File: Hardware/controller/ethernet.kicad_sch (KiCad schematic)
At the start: 18 parts, among them U401 KSZ8041TL, X401 50MHz

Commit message: Controller board fan controller
- Added a fan controller (the same EMC2101-R as on the driver) to the
  controller board, to control the rear case fan. This is driven off the
  rear IO I2C bus, which itself is switched behind the "auxiliary" I2C
  bus.
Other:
- title: Ethernet PHY -> Processor Complex – Ethernet PHY
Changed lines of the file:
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@@
   (paper "A4")
   (title_block
-    (title "Ethernet PHY")
+    (title "Processor Complex – Ethernet PHY")
     (date "2022-03-06")
     (rev "1")

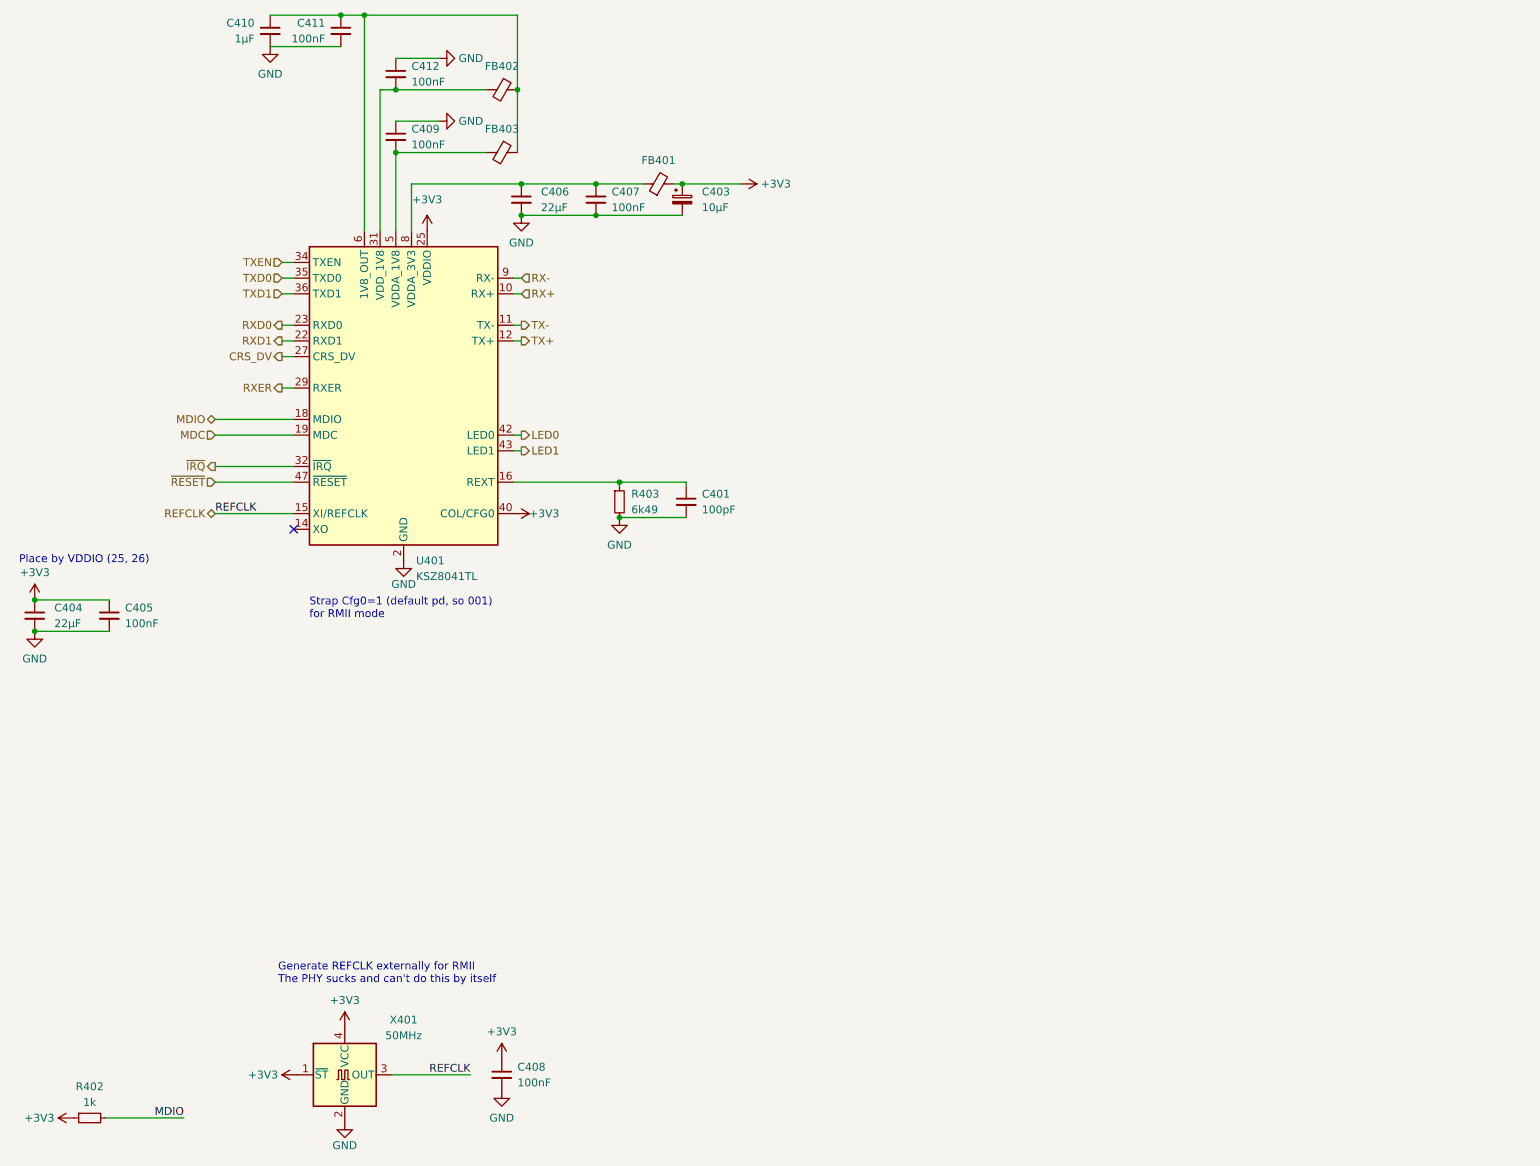
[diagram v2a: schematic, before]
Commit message: Re-design around STM32MP1 (#2)
* Start work on rev3 hardware

- This fits the Technomet R110 enclosure and supports multiple load
  boards, connected via CAN rather than I2C. Each load has a
  microcontroller of its own.

* More new layout stuff

- More work on the new controller board layout

- Rework rear IO board for the new Technomet rear panel (it has an
  expansion connector for CAN also, and features four screw holes
  instead of two)

- Added a few footprints (expansion RJ45 connector; some
  horizontal/vertical headers)

* Work on controller VSense, power

- Routed 3V3 switching supply

- Created footprint and symbols for Kemet EA2 series latching relay

- Added relays to controller to handle routing of voltage sense inputs
  to the sampling ADC

* Rear IO rework

- Mostly finished the rear IO board rework (adding the CAN filtering and
  switchable termination; trigger input pulse shaper; fuses for
  expansion +12V)

- Changed encoder type on front panel for a shorter type

- Created schematic models and footprints for Bournds DR311 chokes;
  Mill-Max 2108 solder turrets

* More work on new controller board

- Switched mains connection for a push-in screw terminal, rather than a
  pluggable block (takes up less space, less parts)

- Added input terminal for rear VSense inputs

- Added -5V supply (same circuit as on analog board; required for
  voltage input sense)

- Replaced beeper with a side-firing version. It takes up a bunch less
  space vertically, and also now added a resistor to (hopefully) make it
  somewhat more quiet

- Added connector for bonus displays

* Add "bonus display" board

- Created the bonus display board, which houses a chip-on-glass 4x10
  text character display. It's meant to be mounted next to the input
  jacks to show a constant location of current/voltage, even if the main
  display is used for menus or other stuff.

- More tweaks to controller board, to do with power g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
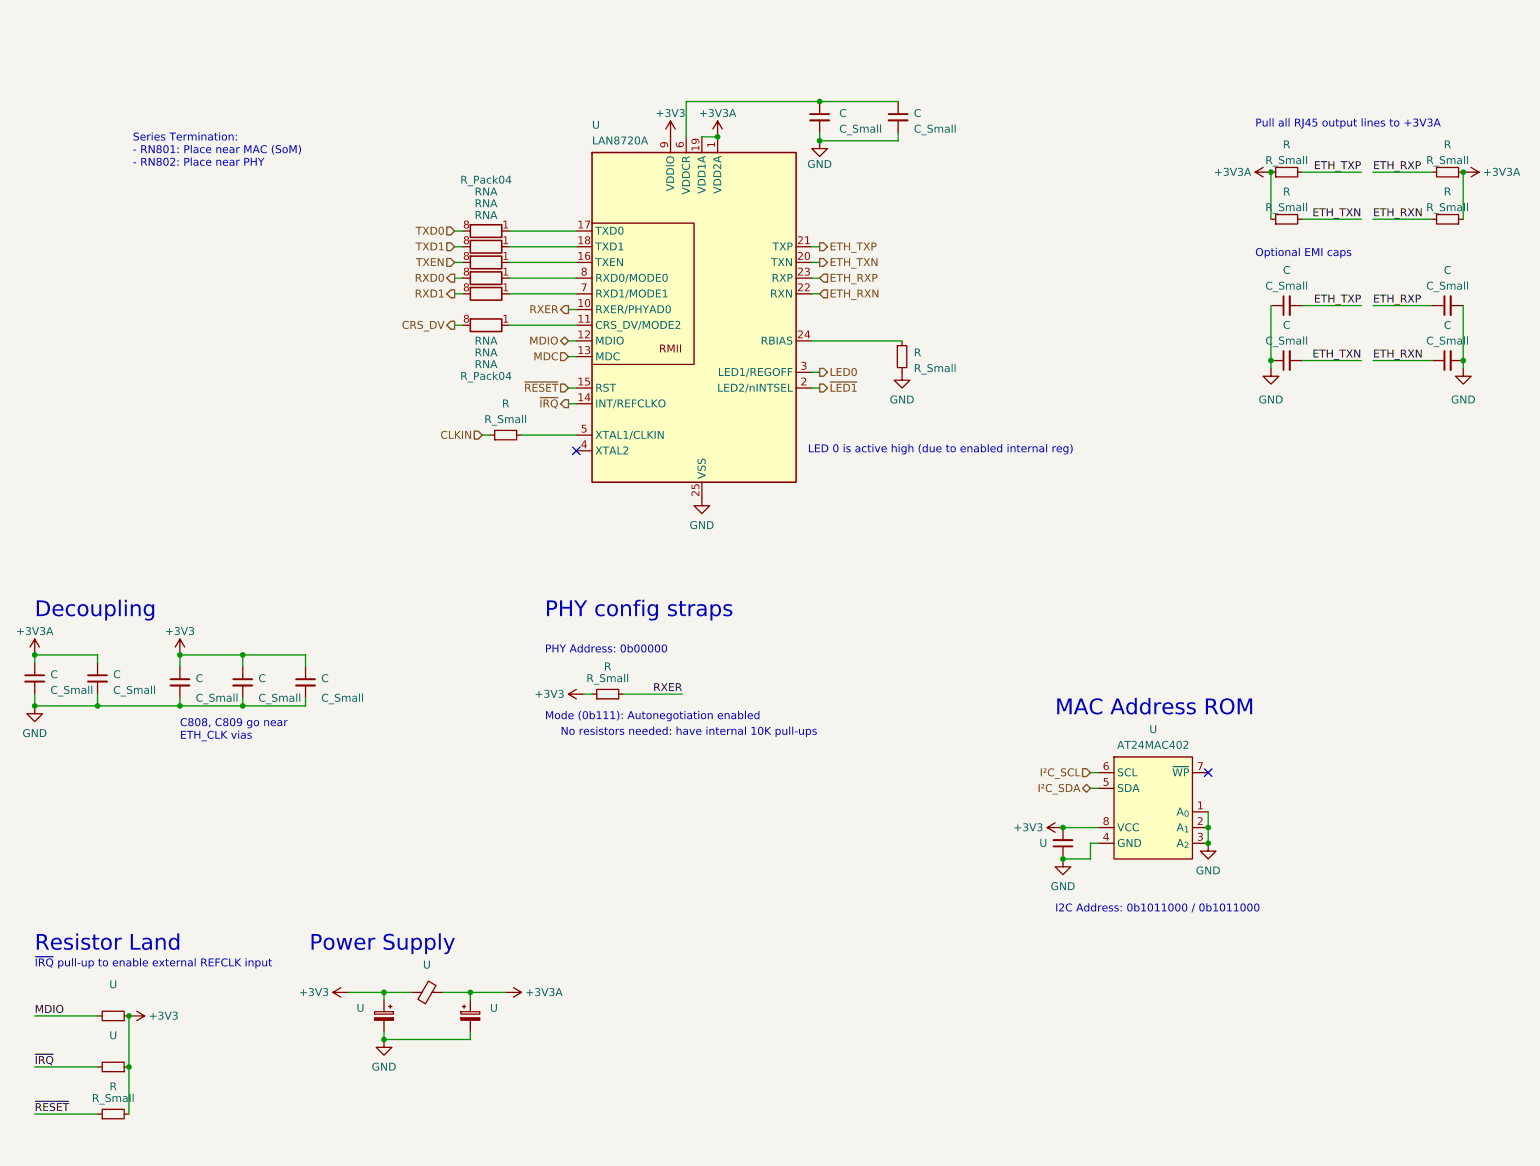
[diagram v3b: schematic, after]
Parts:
- removed C401: 100pF, Capacitor_SMD:C_0805_2012Metric_Pad1.18x1.45mm_HandSolder, symbol Device:C_Small
- removed C403: 10µF, Capacitor_Tantalum_SMD:CP_EIA-3216-18_Kemet-A_Pad1.58x1.35mm_HandSolder, symbol Device:C_Polarized_Small
- removed C404, C406: 22µF, Capacitor_SMD:C_0805_2012Metric_Pad1.18x1.45mm_HandSolder, symbol Device:C_Small
- removed C405, C407, C408, C409, C411, C412: 100nF, Capacitor_SMD:C_0805_2012Metric_Pad1.18x1.45mm_HandSolder, symbol Device:C_Small
- removed C410: 1µF, Capacitor_SMD:C_0805_2012Metric_Pad1.18x1.45mm_HandSolder, symbol Device:C_Small
- removed FB401, FB402, FB403: FerriteBead_Small, Inductor_SMD:L_0805_2012Metric_Pad1.05x1.20mm_HandSolder, symbol Device:FerriteBead_Small
- removed R402: 1k, Resistor_SMD:R_0805_2012Metric_Pad1.20x1.40mm_HandSolder, symbol Device:R_Small
- removed R403: 6k49, Resistor_SMD:R_0805_2012Metric_Pad1.20x1.40mm_HandSolder, symbol Device:R_Small
- removed U401: KSZ8041TL, Package_QFP:TQFP-48_7x7mm_P0.5mm, symbol programmable-load:KSZ8041TL
- removed X401: 50MHz, Oscillator:Oscillator_SMD_SeikoEpson_SG8002LB-4Pin_5.0x3.2mm, symbol Oscillator:SG-5032CAN
- added C (x11): C_Small, symbol Device:C_Small
- added R (x8): R_Small, symbol Device:R_Small
- added RN (x6): R_Pack04, symbol Device:R_Pack04_Split
- added U (x2): (no value), symbol Device:C_Polarized_Small
- added U: LAN8720A, Package_DFN_QFN:QFN-24-1EP_4x4mm_P0.5mm_EP2.6x2.6mm, symbol Interface_Ethernet:LAN8720A
- added U: (no value), symbol Device:FerriteBead_Small
- added U (x2): (no value), symbol Device:R_Small
- added U: (no value), symbol Device:C_Small
- added U: AT24MAC402, Package_SO:TSSOP-8_4.4x3mm_P0.65mm, symbol programmable-load:AT24MAC402
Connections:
- net +3V3: now also C.1, C.1, C.1, R.1, R.2, U.1, U.1, U.1, U.1, U.2, U.8 (VCC), U.9 (VDDIO)
- net CRS_DV: now also RN.8 (R1.2)
- net GND: now also C.1, C.1, C.2, C.2, C.2, C.2, C.2, C.2, C.2, C.2, C.2, R.2, U.1, U.1 (A_{0}), U.2, U.2, U.2 (A_{1}), U.25 (VSS), U.3 (A_{2}), U.4 (GND)
- net LED0: now also U.3 (LED1/REGOFF)
- net MDC: now also U.13 (MDC)
- net MDIO: now also U.12 (MDIO), U.2
- net RXD0: now also RN.8 (R1.2)
- net RXD1: now also RN.8 (R1.2)
- net RXER: now also R.2, U.10 (RXER/PHYAD0)
- net TXD0: now also RN.8 (R1.2)
- net TXD1: now also RN.8 (R1.2)
- net TXEN: now also RN.8 (R1.2)
- net ~{IRQ}: now also U.14 (INT/REFCLKO), U.2
- net ~{RESET}: now also R.1, U.15 (RST)
- new net: R.1, U.24 (RBIAS)
- new net: C.1, C.1, U.6 (VDDCR)
- new net: RN.1 (R1.1), U.11 (CRS_DV/MODE2)
- new net: RN.1 (R1.1), U.16 (TXEN)
- new net: RN.1 (R1.1), U.17 (TXD0)
- new net: RN.1 (R1.1), U.18 (TXD1)
- new net: R.2, U.5 (XTAL1/CLKIN)
- new net: RN.1 (R1.1), U.7 (RXD1/MODE1)
- new net: RN.1 (R1.1), U.8 (RXD0/MODE0)
- new net +3V3A: C.1, C.1, R.1, R.1, R.1, R.1, U.1, U.1 (VDD2A), U.19 (VDD1A), U.2
- new net CLKIN: R.1
- new net ETH_RXN: C.1, R.2, U.22 (RXN)
- new net ETH_RXP: C.1, R.2, U.23 (RXP)
- new net ETH_TXN: C.2, R.2, U.20 (TXN)
- new net ETH_TXP: C.2, R.2, U.21 (TXP)
- new net I²C_SCL : U.6 (SCL)
- new net I²C_SDA: U.5 (SDA)
- new net ~{LED1}: U.2 (LED2/nINTSEL)
- no-connect marks 1 -> 2
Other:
- note added: "C808, C809 go near ETH_CLK vias"
- note added: "Decoupling"
- note added: "I2C Address: 0b1011000 / 0b1011000"
- note added: "LED 0 is active high (due to enabled internal reg)"
- note added: "MAC Address ROM"
- note added: "Mode (0b111): Autonegotiation enabled"
- note added: "No resistors needed: have internal 10K pull-ups"
- note added: "Optional EMI caps"
- note added: "PHY Address: 0b00000"
- note added: "PHY config straps"
- note added: "Power Supply"
- note added: "Pull all RJ45 output lines to +3V3A"
- note added: "Resistor Land"
- note added: "Series Termination: - RN801: Place near MAC (SoM) - RN802: Place near PHY"
- note added: "~{IRQ} pull-up to enable external REFCLK input"
- note removed: "Generate REFCLK externally for RMII The PHY sucks and can't do this by itself"
- note removed: "Place by VDDIO (25, 26)"
- note removed: "Strap Cfg0=1 (default pd, so 001) for RMII mode"
- title: Processor Complex – Ethernet PHY -> (none)
